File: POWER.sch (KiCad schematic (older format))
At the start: 33 parts

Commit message: Schematics:  - Added STZM32 MCU for the CPU kernel  - Added ESP8266 for WiFi Subsheet
Firmware:
 - Generated BIOS configuration for CubeMX
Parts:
- added C?: 100n, symbol C_Small
- added C? (x2): C_Small, symbol C_Small
- added R?: 0, symbol R
- added U?: STM32F439NIH6, symbol STM32F439NIH6
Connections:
- net labels added: +3V3, +BATT
- wire segments 131 -> 145
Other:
- moved on the sheet: C?, L?, R?, U?

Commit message: current version of the schematics. Audio circuits are still missing.
Audio curcuit topology
Audio from cellphone module is routed to STM
Audio from microphone is routed to STM
STM processes audio and routes microphone data to cellphone module
STM processes audio and routes cellphone audio to amplifier
analog multiplexer can switch route from mic directly to cellphone module and module to speaker
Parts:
- added FI401: EMI_FILTER2, symbol EMI_FILTER2
- gave numbers to parts that had none: 38
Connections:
- net labels added: +5V, VCC
- wire segments 145 -> 148

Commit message: added Ti WL1807/1837 Module for WLAN and Bluetooth. added Test Points
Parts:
- added C207, C208, C209, C210, C211, C212, C213, C214, C215, C216, C217, C218, C219, C220, C221, C222, C223, C224, C225: 100n, symbol C_Small
- added TP? (x17): TP, symbol TP
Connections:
- wire segments 148 -> 188
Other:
- moved on the sheet: C403, C408, FI401, L401, R402, R403, R404, R405, R406, R409, R410, U401

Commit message: short schematics review and proposed changes
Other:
- note added: "10uF 0603"
- note added: "TPS61046"
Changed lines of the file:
@@
 	1    0    0    -1
 $EndComp
+Text Notes 6750 2200 0    60   ~ 0
+TPS61046
+Text Notes 2300 3000 0    60   ~ 0
+10uF 0603
 $EndSCHEMATC

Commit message: moved to some Bus routing for serveral communication signals on the top sheet. This reduces lines on the top sheet.
Changed 4V boost converter circuit toi use TPS61046 for size reasons
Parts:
- removed C404: C, symbol CP_Small
- removed C410: C, symbol C_Small
- removed D401: MBR0530, symbol D_Schottky
- removed R411: R, symbol R
- removed TP?: TP, symbol TP
- removed U403: TPS61045, symbol TPS61045
- added C?: 10u, symbol C_Small
- added C?: 100n, symbol C_Small
- added C?: 1n, symbol C_Small
- added U?: TPS61046, symbol TPS61046
- C402: value C -> 10u
- C405: value C -> 100n
- C406: value C -> 1n
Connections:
- wire segments 188 -> 303
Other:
- note removed: "10uF 0603"
- note removed: "TPS61046"
- moved on the sheet: C402, C405, C406, C409, C413, R401, R402, R407, R408, R412, R413, R414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

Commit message: aktuelle Version
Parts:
- removed C401, C407, C414: 1u, symbol CP_Small
- added C229, C230, C231: 1u, Capacitors_SMD:C_0603, symbol C_Small
- added R249: 0, Resistors_SMD:R_0603, symbol R
- C207, C208, C209, C210, C211, C212, C213, C214, C215, C216, C217, C218, C219, C220, C221, C222, C223, C224, C225, C402, C403, C405, C406, C408, C409, C411, C412, C413, C415: footprint (none) -> Capacitors_SMD:C_0603
- C226, C227, C228: renamed from C?; footprint (none) -> Capacitors_SMD:C_0603
- L401, L402, R401, R402, R403, R404, R405, R406, R407, R408, R409, R410, R412, R413, R414, R415, R416: footprint (none) -> Resistors_SMD:R_0603
- TP201, TP202, TP203, TP204, TP205, TP206, TP207, TP208, TP209, TP210, TP211, TP212, TP213, TP214, TP215, TP216: renamed from TP?; footprint (none) -> buttons:TP
- U202: renamed from U?; footprint (none) -> TO_SOT_Packages_SMD:SOT-23-5
- U401: footprint (none) -> SMD_Packages:SOIC-8-N
- U402: footprint (none) -> TO_SOT_Packages_SMD:SOT-23-5
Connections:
- wire segments 303 -> 190

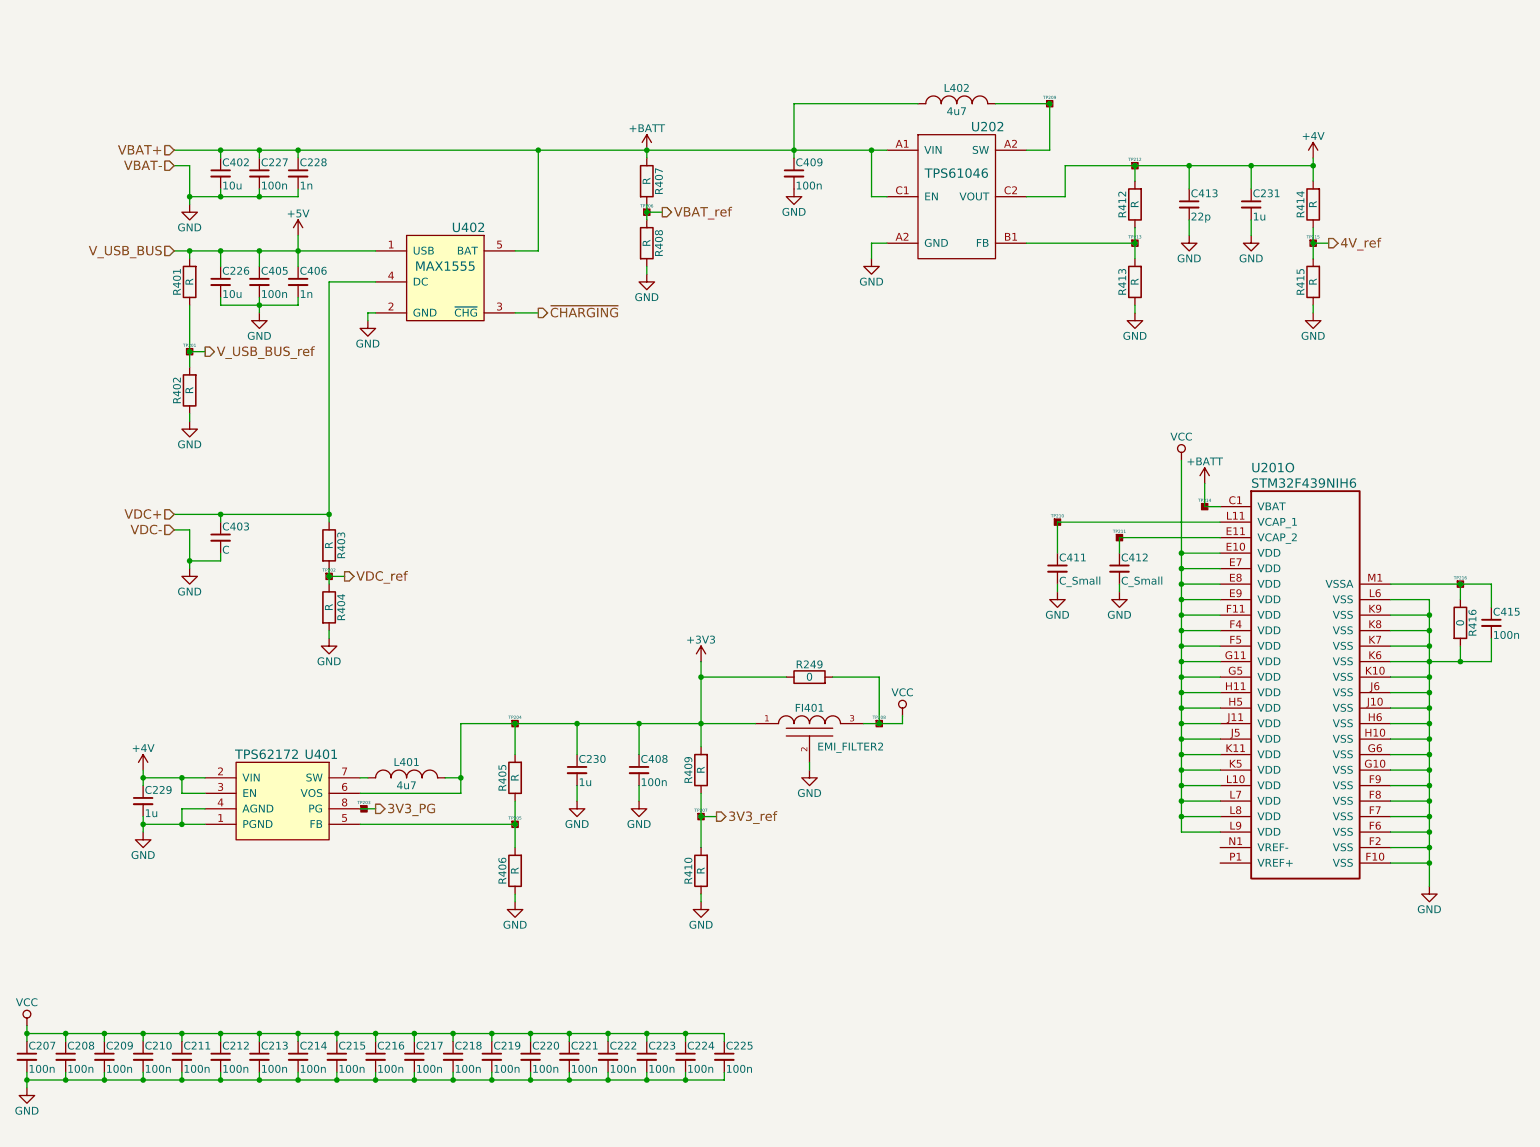
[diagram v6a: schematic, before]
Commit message: display placement
The placement of the display connector is set.
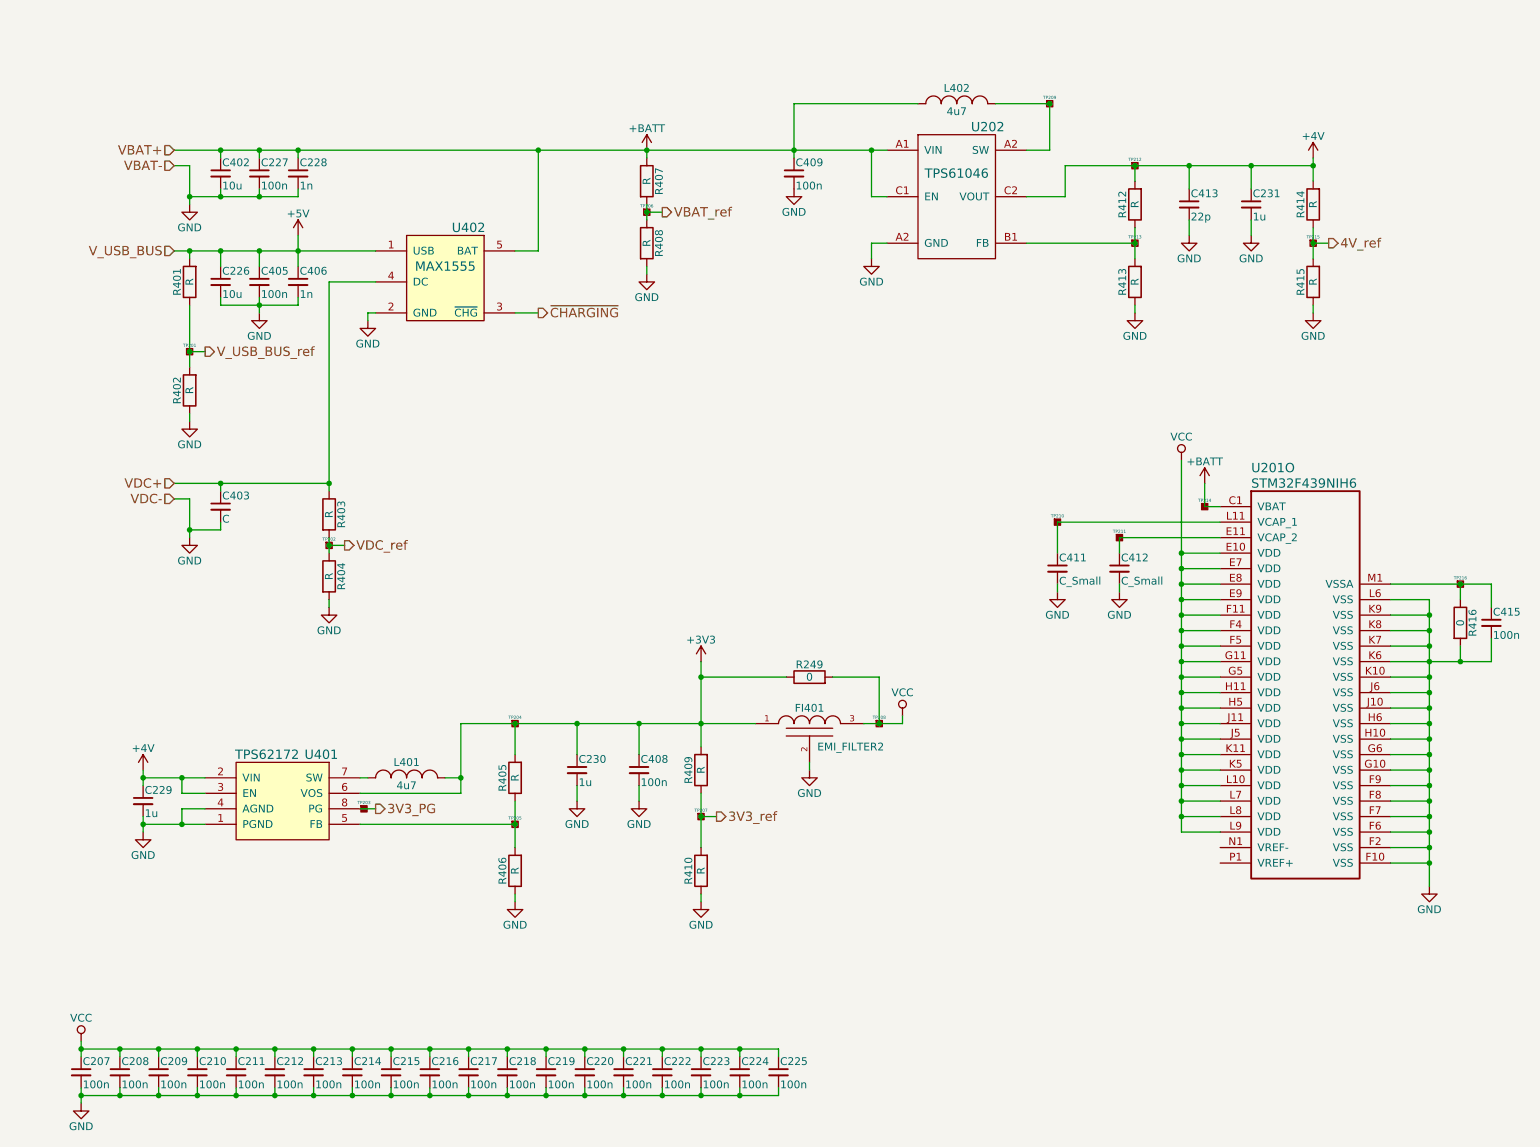
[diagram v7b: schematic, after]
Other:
- moved on the sheet: C207, C208, C209, C210, C211, C212, C213, C214, C215, C216, C217, C218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
